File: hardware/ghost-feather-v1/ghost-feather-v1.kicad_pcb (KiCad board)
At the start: 2 copper layers, 71 parts, among them J1 Conn_ARM_SWD_TagConnect_TC2030, J2 USB_C_Receptacle_USB2.0, J3 Conn_01x03, J4 Conn_01x03, J5 Conn_01x03, J6 Conn_01x03, J7 Conn_01x08, Q1 BSS138, Q2 BSS138, Q3 BSS138, Q4 BSS138, SW2 BOOT0, U1 STM32F722RETx, U2 BMI270, U3 USBLC6-2SC6_MOD, U4 MPM3610, U5 MPM3610, X1 16MHz, X2 32kHz768

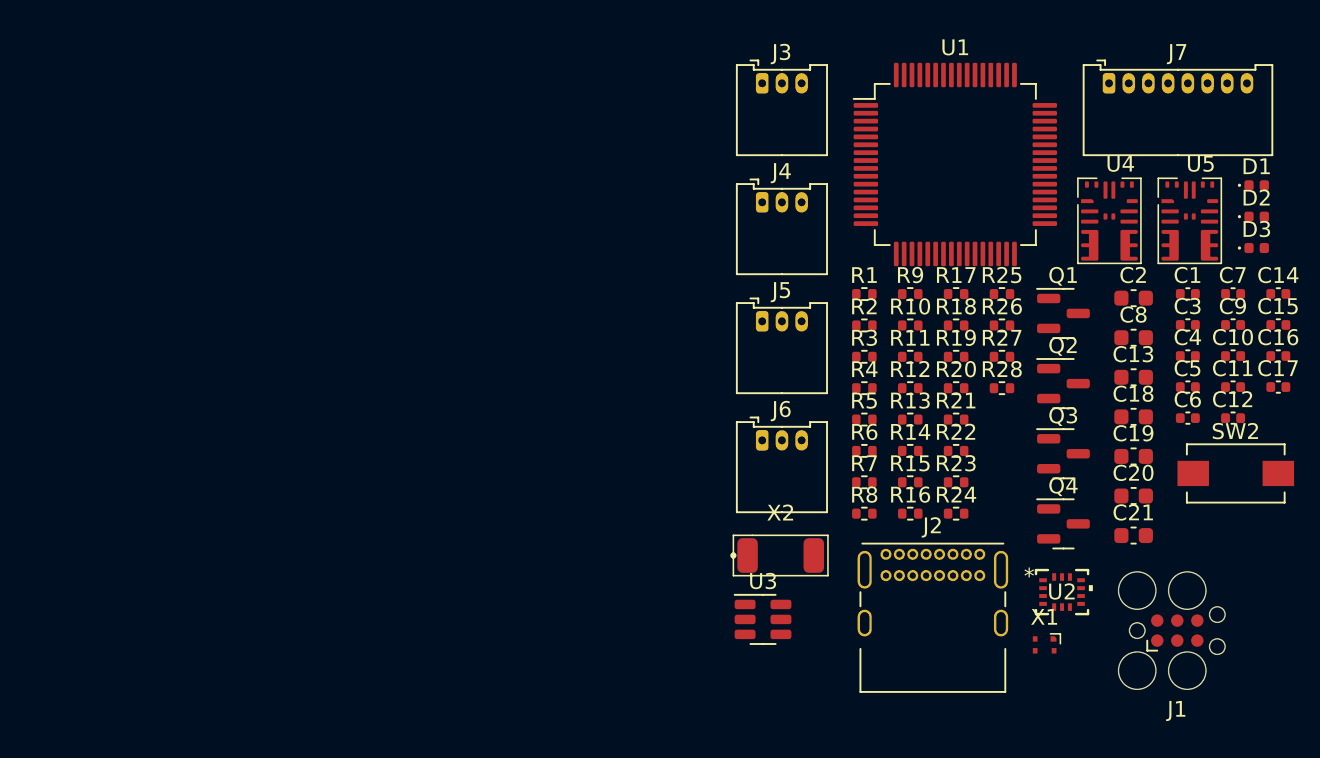
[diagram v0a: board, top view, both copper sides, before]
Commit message: feat: Components placement on PCB #1
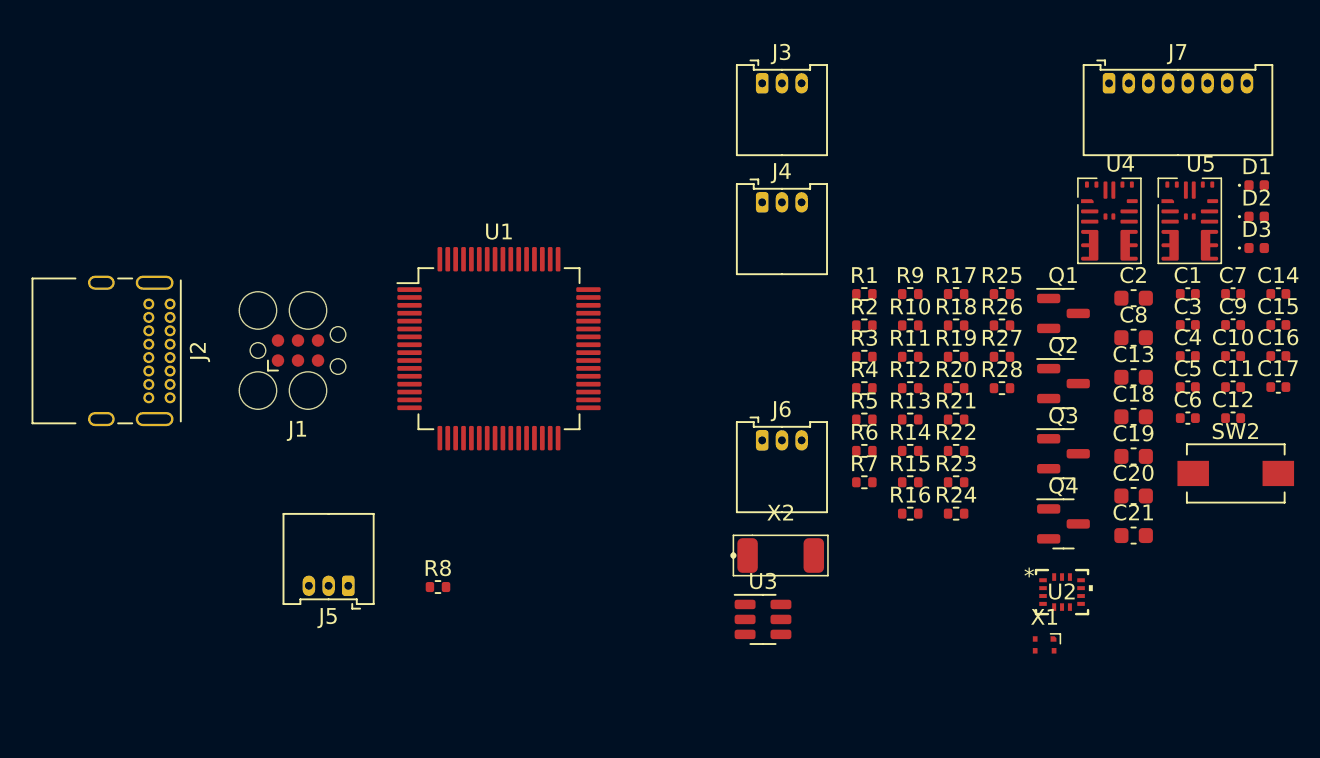
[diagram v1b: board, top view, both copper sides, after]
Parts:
- moved J1 58.5 mm to (82.7, 74.6)
- moved J2 48.1 mm to (74.5, 71.7), turned to -90 degrees
- moved U1 31.2 mm to (95.4, 74.5)
- moved J5 31.2 mm to (85.8, 89.5), turned to 180 degrees
- moved R8 27.4 mm to (91.5, 89.6)
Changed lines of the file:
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@@
   )
   (footprint "Package_QFP:LQFP-64_10x10mm_P0.5mm" (layer "F.Cu")
-    (at 124.35 62.804)
+    (at 95.4 74.49)
     (descr "LQFP, 64 Pin (https://www.analog.com/media/en/technical-documentation/data-sheets/ad7606_7606-6_7606-4.pdf), generated with kicad-footprint-generator ipc_gullwing_generator.py")
     (tags "LQFP QFP")
@@
   )
   (footprint "Resistor_SMD:R_0402_1005Metric" (layer "F.Cu")
-    (at 118.58 84.954)
+    (at 91.53 89.61)
     (descr "Resistor SMD 0402 (1005 Metric), square (rectangular) end terminal, IPC_7351 nominal, (Body size source: IPC-SM-782 page 72, https://www.pcb-3d.com/wordpress/wp-content/uploads/ipc-sm-782a_amendment_1_and_2.pdf), generated with kicad-footprint-generator")
     (tags "resistor")
@@
   )
   (footprint "Connector_USB:USB_C_Receptacle_GCT_USB4085" (layer "F.Cu")
-    (at 119.95 87.534)
+    (at 74.535 71.655 -90)
     (descr "USB 2.0 Type C Receptacle, https://gct.co/Files/Drawings/USB4085.pdf")
     (tags "USB Type-C Receptacle Through-hole Right angle")
@@
     (property "ki_keywords" "usb universal serial bus type-C USB2.0")
     (attr through_hole)
-    (fp_text reference "J2" (at 2.975 -1.8) (layer "F.SilkS")
-        (effects (font (size 1 1) (thickness 0.15)))
-    )
-    (fp_text value "USB_C_Receptacle_USB2.0" (at 2.975 9.925) (layer "F.Fab")
-        (effects (font (size 1 1) (thickness 0.15)))
-    )
-    (fp_text user "PCB Edge" (at 2.975 6.1) (layer "Dwgs.User")
+    (fp_text reference "J2" (at 2.975 -1.8 90) (layer "F.SilkS")
+        (effects (font (size 1 1) (thickness 0.15)))
+    )
+    (fp_text value "USB_C_Receptacle_USB2.0" (at 2.975 9.925 90) (layer "F.Fab")
+        (effects (font (size 1 1) (thickness 0.15)))
+    )
+    (fp_text user "PCB Edge" (at 2.975 6.1 90) (layer "Dwgs.User")
         (effects (font (size 0.5 0.5) (thickness 0.1)))
     )
-    (fp_text user "${REFERENCE}" (at 2.975 4.025) (layer "F.Fab")
+    (fp_text user "${REFERENCE}" (at 2.975 4.025 90) (layer "F.Fab")
         (effects (font (size 1 1) (thickness 0.15)))
     )
@@
     (fp_line (start 7.45 -0.56) (end 7.45 8.61)
       (stroke (width 0.1) (type solid)) (layer "F.Fab"))
-    (pad "A1" thru_hole circle (at 0 0) (size 0.7 0.7) (drill 0.4) (layers "*.Cu" "*.Mask")
+    (pad "A1" thru_hole circle (at 0 0 270) (size 0.7 0.7) (drill 0.4) (layers "*.Cu" "*.Mask")
       (net 2 "GND") (pinfunction "GND") (pintype "passive"))
-    (pad "A4" thru_hole circle (at 0.85 0) (size 0.7 0.7) (drill 0.4) (layers "*.Cu" "*.Mask")
+    (pad "A4" thru_hole circle (at 0.85 0 270) (size 0.7 0.7) (drill 0.4) (layers "*.Cu" "*.Mask")
       (net 8 "+5V") (pinfunction "VBUS") (pintype "passive"))
-    (pad "A5" thru_hole circle (at 1.7 0) (size 0.7 0.7) (drill 0.4) (layers "*.Cu" "*.Mask")
+    (pad "A5" thru_hole circle (at 1.7 0 270) (size 0.7 0.7) (drill 0.4) (layers "*.Cu" "*.Mask")
       (net 16 "Net-(J2-CC1)") (pinfunction "CC1") (pintype "bidirectional"))
-    (pad "A6" thru_hole circle (at 2.55 0) (size 0.7 0.7) (drill 0.4) (layers "*.Cu" "*.Mask")
+    (pad "A6" thru_hole circle (at 2.55 0 270) (size 0.7 0.7) (drill 0.4) (layers "*.Cu" "*.Mask")
       (net 17 "/USBC_DP") (pinfunction "D+") (pintype "bidirectional"))
-    (pad "A7" thru_hole circle (at 3.4 0) (size 0.7 0.7) (drill 0.4) (layers "*.Cu" "*.Mask")
+    (pad "A7" thru_hole circle (at 3.4 0 270) (size 0.7 0.7) (drill 0.4) (layers "*.Cu" "*.Mask")
       (net 18 "/USBC_DM") (pinfunction "D-") (pintype "bidirectional"))
-    (pad "A8" thru_hole circle (at 4.25 0) (size 0.7 0.7) (drill 0.4) (layers "*.Cu" "*.Mask")
+    (pad "A8" thru_hole circle (at 4.25 0 270) (size 0.7 0.7) (drill 0.4) (layers "*.Cu" "*.Mask")
       (net 19 "unconnected-(J2-SBU1-PadA8)") (pinfunction "SBU1") (pintype "bidirectional+no_connect"))
-    (pad "A9" thru_hole circle (at 5.1 0) (size 0.7 0.7) (drill 0.4) (layers "*.Cu" "*.Mask")
+    (pad "A9" thru_hole circle (at 5.1 0 270) (size 0.7 0.7) (drill 0.4) (layers "*.Cu" "*.Mask")
       (net 8 "+5V") (pinfunction "VBUS") (pintype "passive"))
-    (pad "A12" thru_hole circle (at 5.95 0) (size 0.7 0.7) (drill 0.4) (layers "*.Cu" "*.Mask")
+    (pad "A12" thru_hole circle (at 5.95 0 270) (size 0.7 0.7) (drill 0.4) (layers "*.Cu" "*.Mask")
       (net 2 "GND") (pinfunction "GND") (pintype "passive"))
-    (pad "B1" thru_hole circle (at 5.95 1.35) (size 0.7 0.7) (drill 0.4) (layers "*.Cu" "*.Mask")
+    (pad "B1" thru_hole circle (at 5.95 1.35 270) (size 0.7 0.7) (drill 0.4) (layers "*.Cu" "*.Mask")
       (net 2 "GND") (pinfunction "GND") (pintype "passive"))
-    (pad "B4" thru_hole circle (at 5.1 1.35) (size 0.7 0.7) (drill 0.4) (layers "*.Cu" "*.Mask")
+    (pad "B4" thru_hole circle (at 5.1 1.35 270) (size 0.7 0.7) (drill 0.4) (layers "*.Cu" "*.Mask")
       (net 8 "+5V") (pinfunction "VBUS") (pintype "passive"))
-    (pad "B5" thru_hole circle (at 4.25 1.35) (size 0.7 0.7) (drill 0.4) (layers "*.Cu" "*.Mask")
+    (pad "B5" thru_hole circle (at 4.25 1.35 270) (size 0.7 0.7) (drill 0.4) (layers "*.Cu" "*.Mask")
       (net 20 "Net-(J2-CC2)") (pinfunction "CC2") (pintype "bidirectional"))
-    (pad "B6" thru_hole circle (at 3.4 1.35) (size 0.7 0.7) (drill 0.4) (layers "*.Cu" "*.Mask")
+    (pad "B6" thru_hole circle (at 3.4 1.35 270) (size 0.7 0.7) (drill 0.4) (layers "*.Cu" "*.Mask")
       (net 17 "/USBC_DP") (pinfunction "D+") (pintype "bidirectional"))
-    (pad "B7" thru_hole circle (at 2.55 1.35) (size 0.7 0.7) (drill 0.4) (layers "*.Cu" "*.Mask")
+    (pad "B7" thru_hole circle (at 2.55 1.35 270) (size 0.7 0.7) (drill 0.4) (layers "*.Cu" "*.Mask")
       (net 18 "/USBC_DM") (pinfunction "D-") (pintype "bidirectional"))
-    (pad "B8" thru_hole circle (at 1.7 1.35) (size 0.7 0.7) (drill 0.4) (layers "*.Cu" "*.Mask")
+    (pad "B8" thru_hole circle (at 1.7 1.35 270) (size 0.7 0.7) (drill 0.4) (layers "*.Cu" "*.Mask")
       (net 21 "unconnected-(J2-SBU2-PadB8)") (pinfunction "SBU2") (pintype "bidirectional+no_connect"))
-    (pad "B9" thru_hole circle (at 0.85 1.35) (size 0.7 0.7) (drill 0.4) (layers "*.Cu" "*.Mask")
+    (pad "B9" thru_hole circle (at 0.85 1.35 270) (size 0.7 0.7) (drill 0.4) (layers "*.Cu" "*.Mask")
       (net 8 "+5V") (pinfunction "VBUS") (pintype "passive"))
-    (pad "B12" thru_hole circle (at 0 1.35) (size 0.7 0.7) (drill 0.4) (layers "*.Cu" "*.Mask")
+    (pad "B12" thru_hole circle (at 0 1.35 270) (size 0.7 0.7) (drill 0.4) (layers "*.Cu" "*.Mask")
       (net 2 "GND") (pinfunction "GND") (pintype "passive"))
-    (pad "S1" thru_hole oval (at -1.35 0.98) (size 0.9 2.4) (drill oval 0.6 2.1) (layers "*.Cu" "*.Mask")
+    (pad "S1" thru_hole oval (at -1.35 0.98 270) (size 0.9 2.4) (drill oval 0.6 2.1) (layers "*.Cu" "*.Mask")
       (net 2 "GND") (pinfunction "SHIELD") (pintype "passive"))
-    (pad "S1" thru_hole oval (at -1.35 4.36) (size 0.9 1.7) (drill oval 0.6 1.4) (layers "*.Cu" "*.Mask")
+    (pad "S1" thru_hole oval (at -1.35 4.36 270) (size 0.9 1.7) (drill oval 0.6 1.4) (layers "*.Cu" "*.Mask")
       (net 2 "GND") (pinfunction "SHIELD") (pintype "passive"))
-    (pad "S1" thru_hole oval (at 7.3 0.98) (size 0.9 2.4) (drill oval 0.6 2.1) (layers "*.Cu" "*.Mask")
+    (pad "S1" thru_hole oval (at 7.3 0.98 270) (size 0.9 2.4) (drill oval 0.6 2.1) (layers "*.Cu" "*.Mask")
       (net 2 "GND") (pinfunction "SHIELD") (pintype "passive"))
-    (pad "S1" thru_hole oval (at 7.3 4.36) (size 0.9 1.7) (drill oval 0.6 1.4) (layers "*.Cu" "*.Mask")
+    (pad "S1" thru_hole oval (at 7.3 4.36 270) (size 0.9 1.7) (drill oval 0.6 1.4) (layers "*.Cu" "*.Mask")
       (net 2 "GND") (pinfunction "SHIELD") (pintype "passive"))
     (model "${KICAD6_3DMODEL_DIR}/Connector_USB.3dshapes/USB_C_Receptacle_GCT_USB4085.wrl"
@@
   )
   (footprint "Connector_Molex:Molex_PicoBlade_53048-0310_1x03_P1.25mm_Horizontal" (layer "F.Cu")
-    (at 112.1 72.754)
+    (at 85.84 89.53 180)
     (descr "Molex PicoBlade Connector System, 53048-0310, 3 Pins per row (http://www.molex.com/pdm_docs/sd/530480210_sd.pdf), generated with kicad-footprint-generator")
     (tags "connector Molex PicoBlade top entry")
@@
     (fp_line (start 4 4.45) (end 1.25 4.45)
       (stroke (width 0.1) (type solid)) (layer "F.Fab"))
-    (pad "1" thru_hole roundrect (at 0 0) (size 0.8 1.3) (drill 0.5) (layers "*.Cu" "*.Mask") (roundrect_rratio 0.25)
+    (pad "1" thru_hole roundrect (at 0 0 180) (size 0.8 1.3) (drill 0.5) (layers "*.Cu" "*.Mask") (roundrect_rratio 0.25)
       (net 2 "GND") (pinfunction "Pin_1") (pintype "passive"))
-    (pad "2" thru_hole oval (at 1.25 0) (size 0.8 1.3) (drill 0.5) (layers "*.Cu" "*.Mask")
+    (pad "2" thru_hole oval (at 1.25 0 180) (size 0.8 1.3) (drill 0.5) (layers "*.Cu" "*.Mask")
       (net 24 "Net-(J5-Pin_2)") (pinfunction "Pin_2") (pintype "passive"))
-    (pad "3" thru_hole oval (at 2.5 0) (size 0.8 1.3) (drill 0.5) (layers "*.Cu" "*.Mask")
+    (pad "3" thru_hole oval (at 2.5 0 180) (size 0.8 1.3) (drill 0.5) (layers "*.Cu" "*.Mask")
       (net 8 "+5V") (pinfunction "Pin_3") (pintype "passive"))
     (model "${KICAD6_3DMODEL_DIR}/Connector_Molex.3dshapes/Molex_PicoBlade_53048-0310_1x03_P1.25mm_Horizontal.wrl"
@@
   )
   (footprint "Connector:Tag-Connect_TC2030-IDC-FP_2x03_P1.27mm_Vertical" (layer "F.Cu")
-    (at 138.43 92.374)
+    (at 82.65 74.605)
     (descr "Tag-Connect programming header; http://www.tag-connect.com/Materials/TC2030-IDC.pdf")
     (tags "tag connect programming header pogo pins")
@@
       (polygon
         (pts
-          (xy 139.7 91.739)
-          (xy 137.16 91.739)
-          (xy 137.16 93.009)
-          (xy 139.7 93.009)
+          (xy 83.92 73.97)
+          (xy 81.38 73.97)
+          (xy 81.38 75.24)
+          (xy 83.92 75.24)
         )
       )

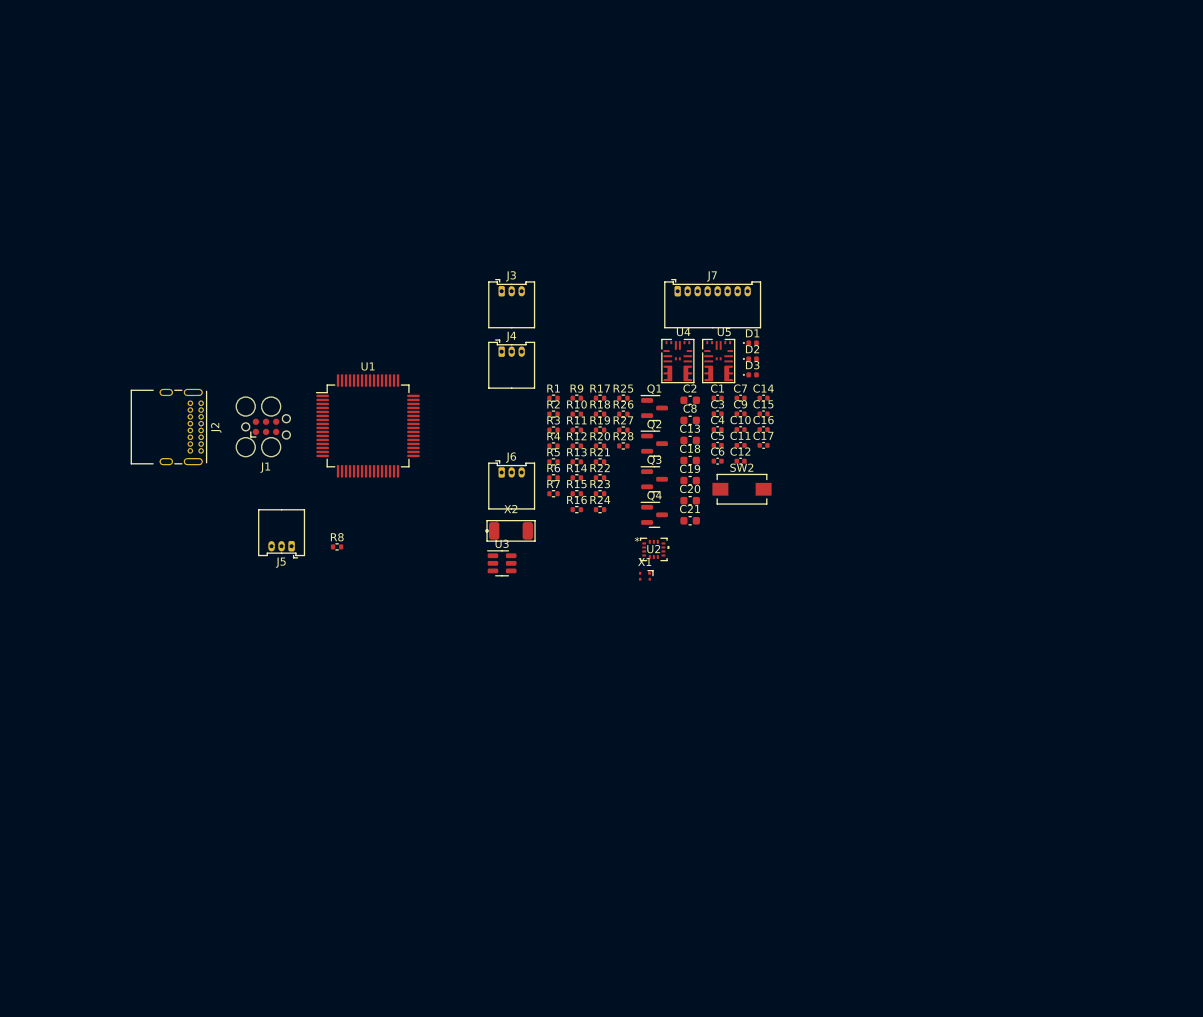
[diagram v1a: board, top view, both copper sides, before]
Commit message: feat: Add f450 frame silkscreen
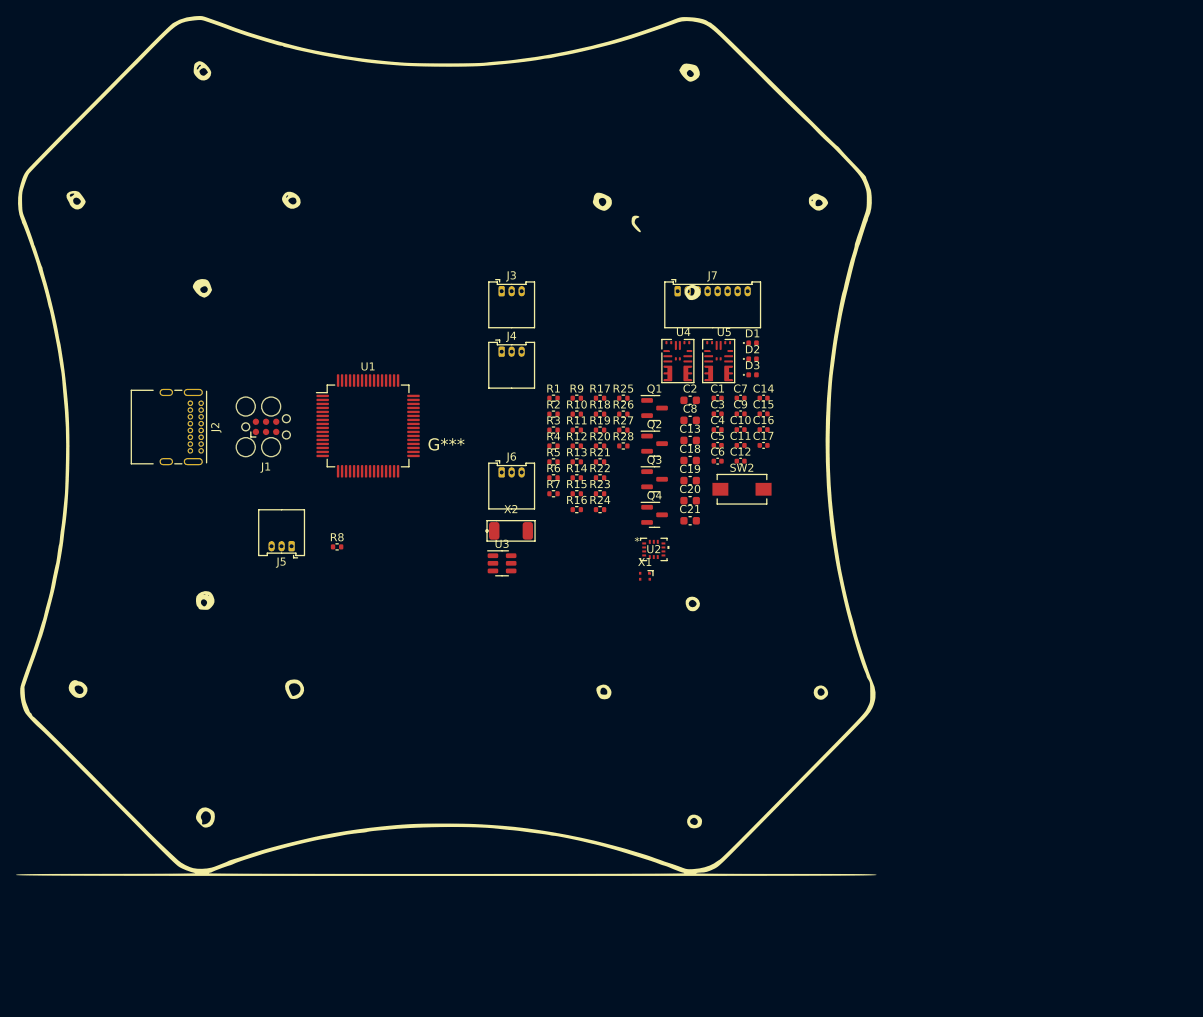
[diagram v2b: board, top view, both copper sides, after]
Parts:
- added G***: LOGO, ghost-feather-v1:f450_04192025, F.Cu at (105.2, 76.8)

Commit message: feat: Add design rules
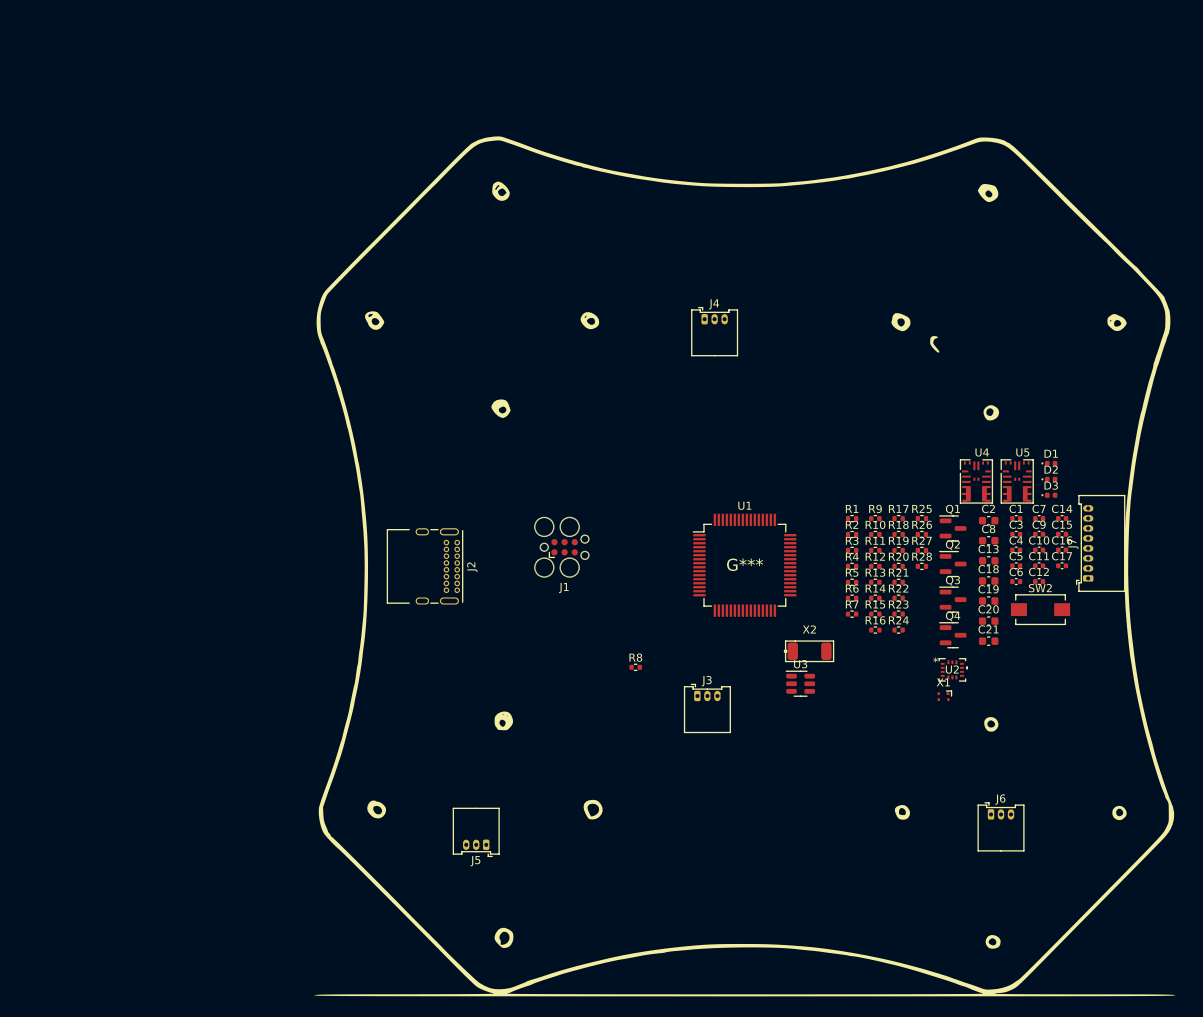
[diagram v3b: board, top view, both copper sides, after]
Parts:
- moved J6 74.6 mm to (173.3, 123.0)
- moved J7 62.6 mm to (185.4, 93.5), turned to 90 degrees
- moved J3 56.2 mm to (136.6, 108.2)
- moved U1 50.2 mm to (142.5, 91.9)
- moved J5 44.6 mm to (110.2, 126.8)
- moved SW2 40.2 mm to (179.5, 97.5)
- moved X1 40.2 mm to (167.3, 108.3)
- moved R1 40.2 mm to (155.9, 86.1)
- moved R10 40.2 mm to (158.8, 88.1)
- moved R11 40.2 mm to (158.8, 90.1)
- moved R12 40.2 mm to (158.8, 92.0)
- moved R13 40.2 mm to (158.8, 94.0)
- moved R14 40.2 mm to (158.8, 96.0)
- moved R15 40.2 mm to (158.8, 98.0)
- moved R16 40.2 mm to (158.8, 100.0)
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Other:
- copper layers 2 -> 4
